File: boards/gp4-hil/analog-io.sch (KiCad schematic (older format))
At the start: 155 parts, among them U10 AD9609, U11 DAC084S085, U12 DAC084S085, U13 DAC084S085, U14 DAC084S085, U19 TS3A4751, U2 XC7A100T-1FTG256C, U25 TS3A4751, U26 TS3A4751, U27 TS3A4751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

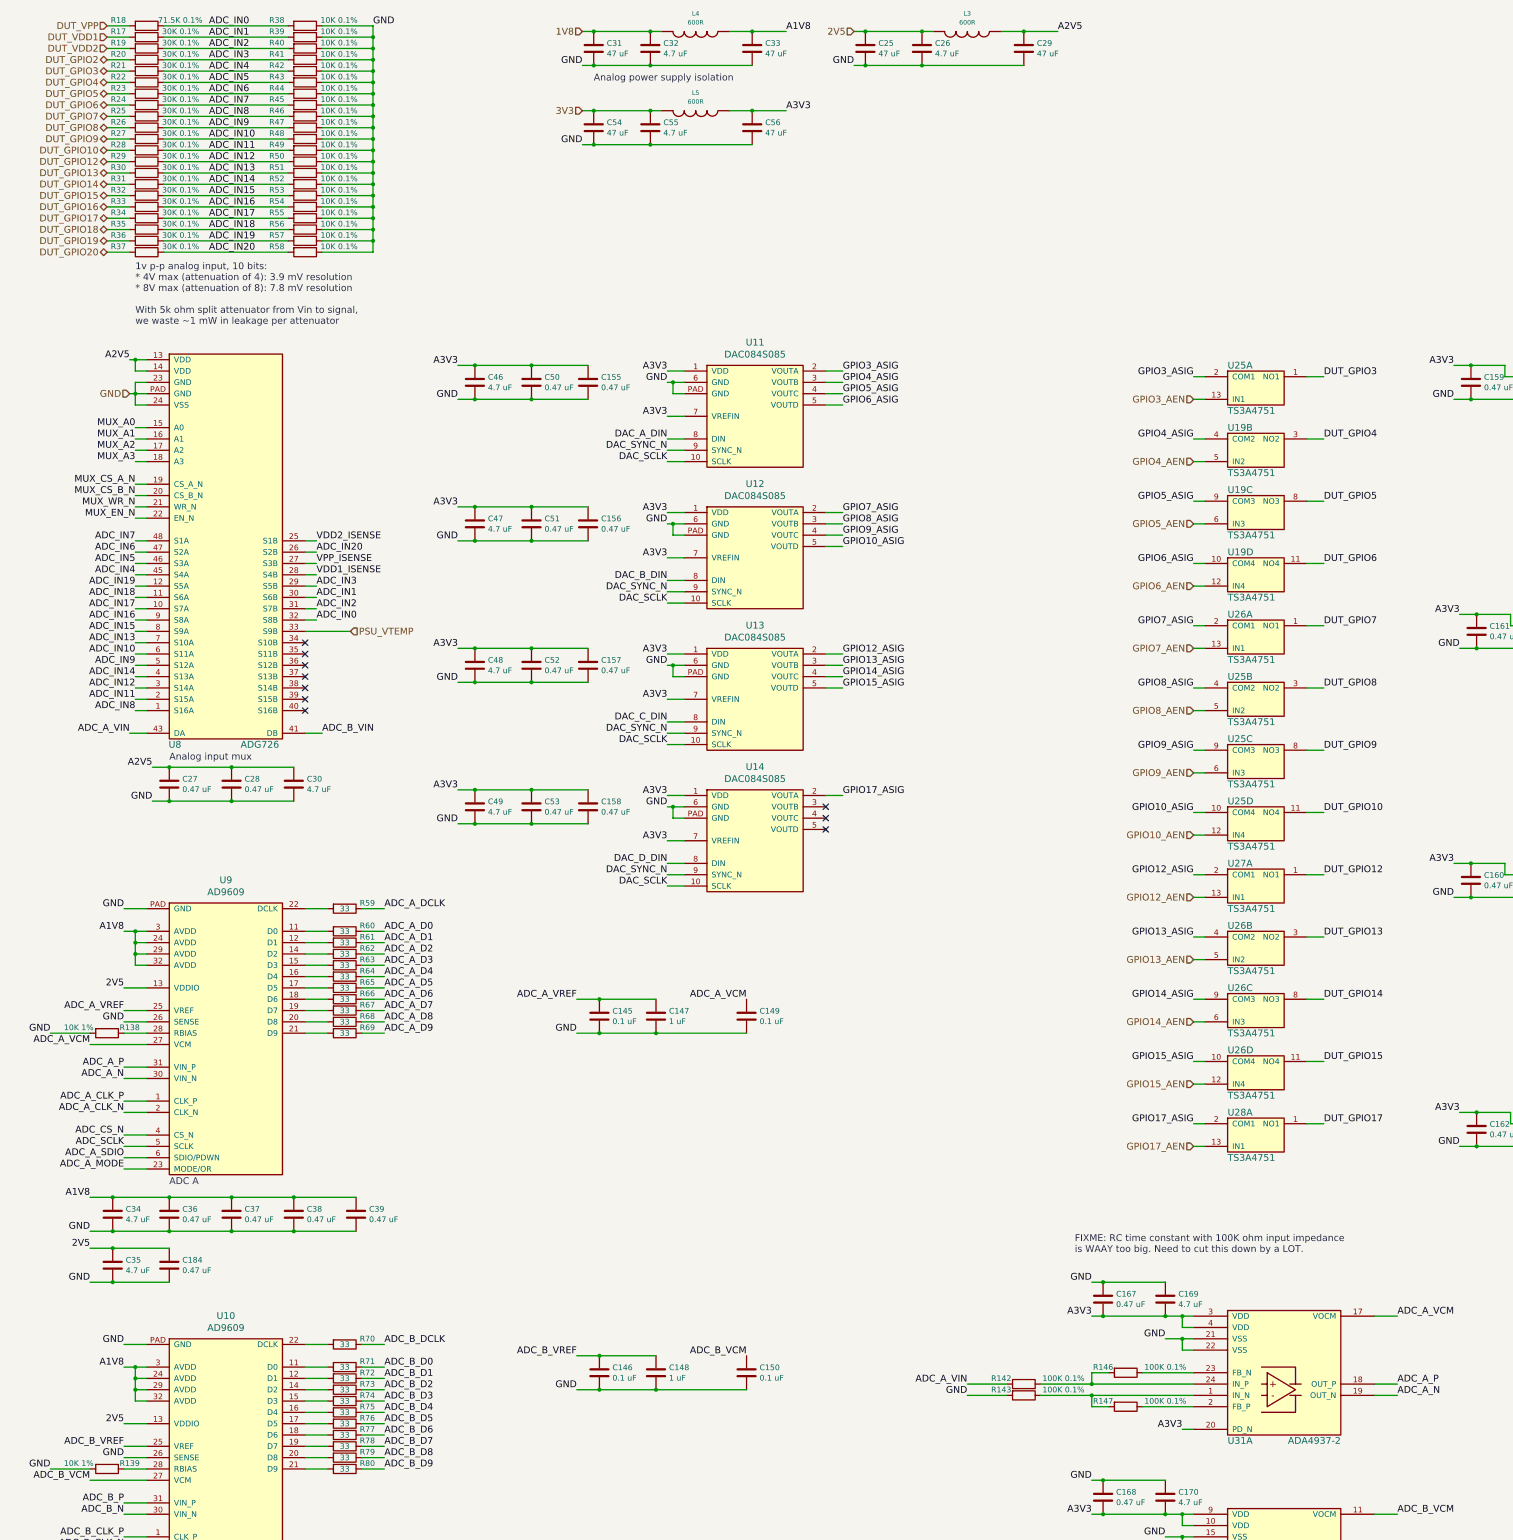
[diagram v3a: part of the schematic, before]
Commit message: Massive cleanup of analog input logic. Deleted a couple dozen components, got higher input bandwidth, reduced BOM cost. What's not to like?
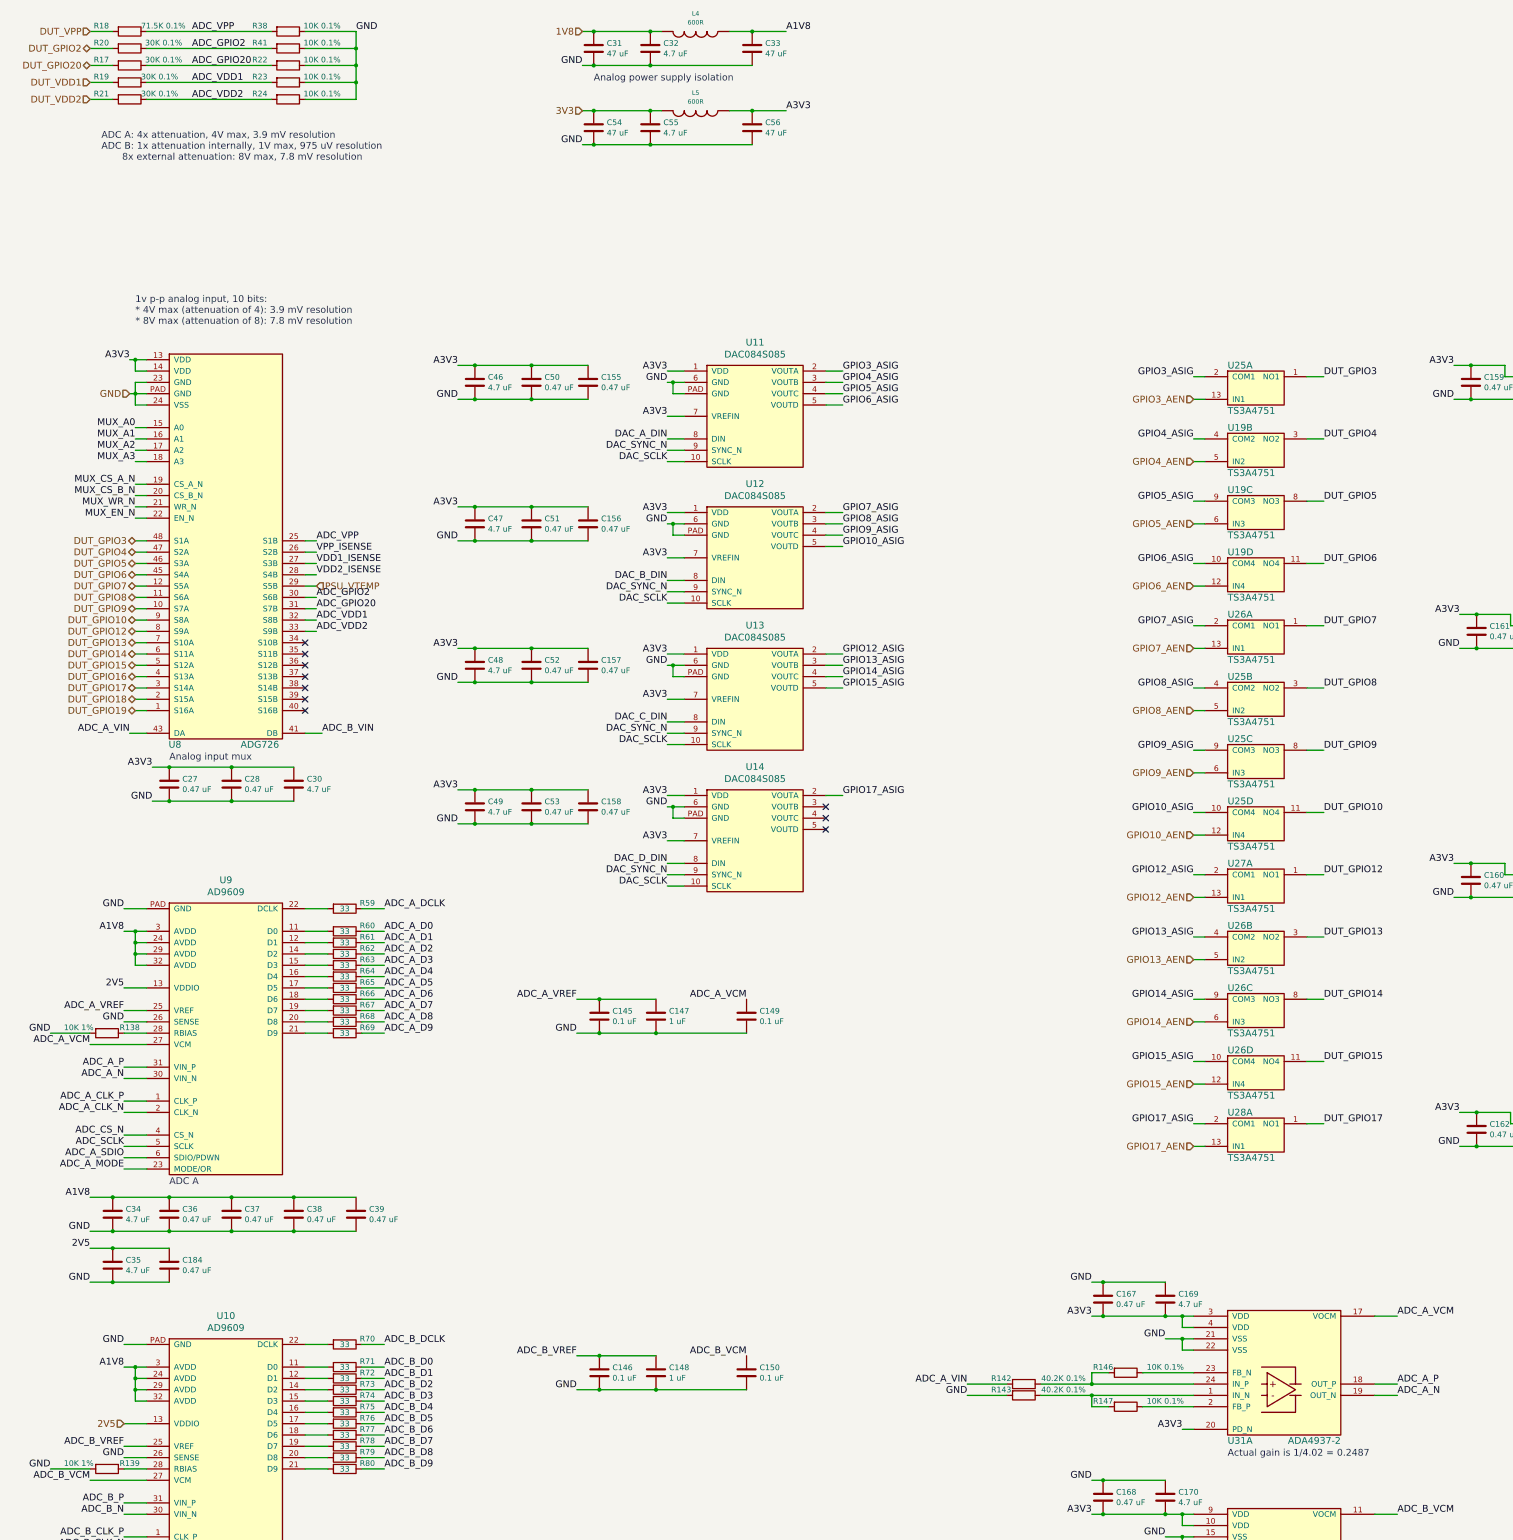
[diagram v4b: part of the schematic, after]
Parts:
- removed C25, C29: 47 uF, azonenberg_pcb:EIA_1206_CAP_NOSILK, symbol C
- removed C26: 4.7 uF, azonenberg_pcb:EIA_0603_CAP_NOSILK, symbol C
- removed L3: 600R, azonenberg_pcb:EIA_0603_INDUCTOR_NOSILK, symbol INDUCTOR_PWROUT
- removed R25, R26, R27, R28, R29, R30, R31, R32, R33, R34, R35, R36, R37: 30K 0.1%, azonenberg_pcb:EIA_0402_RES_NOSILK, symbol R
- removed R39, R40, R42, R43, R44, R45, R46, R47, R48, R49, R50, R51, R52, R53, R54, R55, R56, R57, R58: 10K 0.1%, azonenberg_pcb:EIA_0402_RES_NOSILK, symbol R
- R142, R143: value 100K 0.1% -> 40.2K 0.1%
- R146, R147: value 100K 0.1% -> 10K 0.1%
- R22, R23, R24: value 30K 0.1% -> 10K 0.1%
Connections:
- net A2V5 is gone; now on net A3V3: C27.1, C28.1, C30.1, U8.13 (VDD), U8.14 (VDD)
- net ADC_IN10 is gone; now on net DUT_GPIO14: U8.6 (S11A)
- net ADC_IN11 is gone; now on net DUT_GPIO18: U8.2 (S15A)
- net ADC_IN12 is gone; now on net DUT_GPIO17: U8.3 (S14A)
- net ADC_IN13 is gone; now on net DUT_GPIO13: U8.7 (S10A)
- net ADC_IN14 is gone; now on net DUT_GPIO16: U8.4 (S13A)
- net ADC_IN15 is gone; now on net DUT_GPIO12: U8.8 (S9A)
- net ADC_IN16 is gone; now on net DUT_GPIO10: U8.9 (S8A)
- net ADC_IN17 is gone; now on net DUT_GPIO9: U8.10 (S7A)
- net ADC_IN18 is gone; now on net DUT_GPIO8: U8.11 (S6A)
- net ADC_IN19 is gone; now on net DUT_GPIO7: U8.12 (S5A)
- net ADC_IN20 is gone; now on net VPP_ISENSE: U8.26 (S2B)
- net ADC_IN8 is gone; now on net DUT_GPIO19: U8.1 (S16A)
- net ADC_IN9 is gone; now on net DUT_GPIO15: U8.5 (S12A)
- net DUT_GPIO20: now also R17.2
- net DUT_GPIO3: now also U8.48 (S1A); no longer R21.2
- net DUT_GPIO4: now also U8.47 (S2A); no longer R22.2
- net DUT_GPIO5: now also U8.46 (S3A); no longer R23.2
- net DUT_GPIO6: now also U8.45 (S4A); no longer R24.2
- net DUT_VDD1: now also R19.2; no longer R17.2
- net DUT_VDD2: now also R21.2; no longer R19.2
- net GND: now also R22.1, R23.1, R24.1
- net PSU_VTEMP: now also U8.29 (S5B); no longer U8.33 (S9B)
- net VDD1_ISENSE: now also U8.27 (S3B); no longer U8.28 (S4B)
- net VDD2_ISENSE: now also U8.28 (S4B); no longer U8.25 (S1B)
- net VPP_ISENSE: no longer U8.27 (S3B)
- net ADC_IN0 renamed ADC_VPP
- net ADC_VPP: now also U8.25 (S1B); no longer U8.32 (S8B)
- net ADC_IN1 renamed ADC_GPIO2
- net ADC_GPIO2: now also R20.1, R41.2; no longer R17.1
- net ADC_IN2 renamed ADC_GPIO20
- net ADC_GPIO20: now also R17.1, R22.2; no longer R19.1
- removed net ADC_IN3: R20.1, R41.2, U8.29 (S5B)
- net ADC_IN4 renamed ADC_VDD2
- net ADC_VDD2: now also R24.2, U8.33 (S9B); no longer U8.45 (S4A)
- removed net ADC_IN5: R22.1, U8.46 (S3A)
- removed net ADC_IN6: R23.1, U8.47 (S2A)
- removed net ADC_IN7: R24.1, U8.48 (S1A)
- new net ADC_VDD1: R19.1, R23.2, U8.32 (S8B)
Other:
- note added: "1v p-p analog input, 10 bits:\n* 4V max (attenuation of 4): 3.9 mV resolution\n* 8V max (attenuation of 8): 7.8 mV resolution"
- note added: "ADC A: 4x attenuation, 4V max, 3.9 mV resolution\nADC B: 1x attenuation internally, 1V max, 975 uV resolution\n 8x external attenuation: 8V max, 7.8 mV resolution"
- note added: "Actual gain is 1/4.02 = 0.2487"
- note removed: "1v p-p analog input, 10 bits:\n* 4V max (attenuation of 4): 3.9 mV resolution\n* 8V max (attenuation of 8): 7.8 mV resolution\n\nWith 5k ohm split attenuator from Vin to signal,\nwe waste ~~1 mW in leakage per attenuator"
- note removed: "FIXME: RC time constant with 100K ohm input impedance\nis WAAY too big. Need to cut this down by a LOT."
- moved on the sheet: R18, R20, R38, R41

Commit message: Lots of layout on ADC A among other things
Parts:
- R144, R145, R148, R149: value 100K 0.1% -> 10K 0.1%
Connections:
- net ADC_GPIO2: now also U8.29 (S5B); no longer U8.30 (S6B)
- net ADC_GPIO20: now also U8.30 (S6B); no longer U8.31 (S7B)
- net ADC_VDD1: now also U8.31 (S7B); no longer U8.32 (S8B)
- net ADC_VDD2: now also U8.32 (S8B); no longer U8.33 (S9B)
- net PSU_VTEMP: now also U8.33 (S9B); no longer U8.29 (S5B)
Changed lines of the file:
@@
 Sheet 5 7
 Title "GreenPak Hardware-In-Loop Test Platform"
-Date "2016-06-02"
+Date "2016-06-04"
 Rev "0.1"
 Comp "Andrew Zonenberg"
@@
 NoConn ~ 7650 7800
 NoConn ~ 7650 7600
-Text HLabel 3150 5650 2    60   Input ~ 0
+Text HLabel 3150 6050 2    60   Input ~ 0
 PSU_VTEMP
 $Comp
@@
 P 10300 14350
 F 0 "R148" V 10250 14150 50  0000 C CNN
-F 1 "100K 0.1%" V 10250 14700 50  0000 C CNN
+F 1 "10K 0.1%" V 10250 14700 50  0000 C CNN
 F 2 "azonenberg_pcb:EIA_0402_RES_NOSILK" V 10230 14350 30  0001 C CNN
 F 3 "" H 10300 14350 30  0000 C CNN
@@
 P 9400 14450
 F 0 "R144" V 9350 14250 50  0000 C CNN
-F 1 "100K 0.1%" V 9350 14800 50  0000 C CNN
+F 1 "10K 0.1%" V 9350 14800 50  0000 C CNN
 F 2 "azonenberg_pcb:EIA_0402_RES_NOSILK" V 9330 14450 30  0001 C CNN
 F 3 "" H 9400 14450 30  0000 C CNN
@@
 P 9400 14550
 F 0 "R145" V 9350 14350 50  0000 C CNN
-F 1 "100K 0.1%" V 9350 14900 50  0000 C CNN
+F 1 "10K 0.1%" V 9350 14900 50  0000 C CNN
 F 2 "azonenberg_pcb:EIA_0402_RES_NOSILK" V 9330 14550 30  0001 C CNN
 F 3 "" H 9400 14550 30  0000 C CNN
@@
 P 10300 14650
 F 0 "R149" V 10250 14450 50  0000 C CNN
-F 1 "100K 0.1%" V 10250 15000 50  0000 C CNN
+F 1 "10K 0.1%" V 10250 15000 50  0000 C CNN
 F 2 "azonenberg_pcb:EIA_0402_RES_NOSILK" V 10230 14650 30  0001 C CNN
 F 3 "" H 10300 14650 30  0000 C CNN
@@
 Connection ~ 3500 1050
 Connection ~ 3500 1200
+Text Label 3150 5650 0    60   ~ 0
+ADC_GPIO2
 Text Label 3150 5750 0    60   ~ 0
-ADC_GPIO2
+ADC_GPIO20
 Text Label 3150 5850 0    60   ~ 0
-ADC_GPIO20
+ADC_VDD1
 Text Label 3150 5950 0    60   ~ 0
-ADC_VDD1
-Text Label 3150 6050 0    60   ~ 0
 ADC_VDD2
 Wire Wire Line
